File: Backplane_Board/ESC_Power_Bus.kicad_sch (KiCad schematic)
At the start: 18 parts, among them J21 Conn_01x02_Pin, SW2 SW_DPST_x2

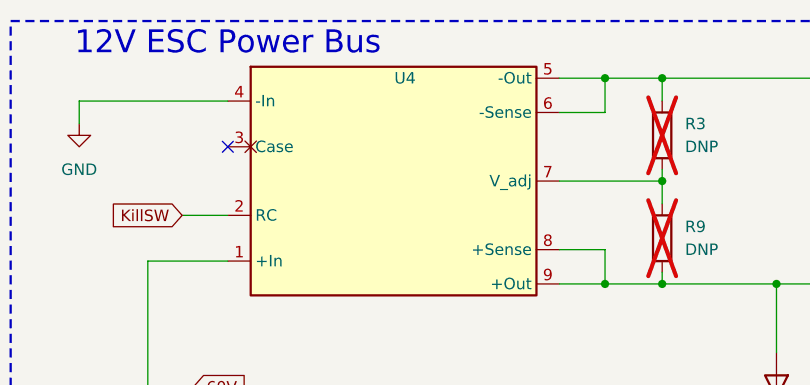
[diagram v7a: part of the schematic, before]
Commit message: updated i2c pullups to 3V3 logic, not isolator needed
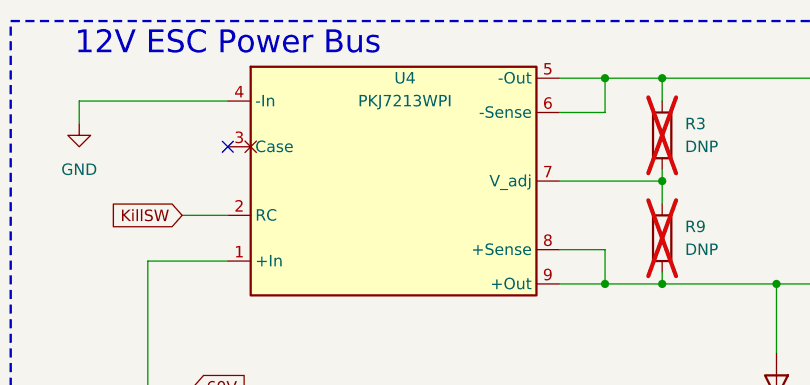
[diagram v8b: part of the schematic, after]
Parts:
- J21: footprint (none) -> Connector_PinHeader_2.54mm:PinHeader_1x02_P2.54mm_Vertical
- SW2: footprint (none) -> TerminalBlock:TerminalBlock_Xinya_XY308-2.54-2P_1x02_P2.54mm_Horizontal
- U4: value ~ -> PKJ7213WPI
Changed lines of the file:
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@@
 			)
 		)
-		(property "Footprint" ""
+		(property "Footprint" "TerminalBlock:TerminalBlock_Xinya_XY308-2.54-2P_1x02_P2.54mm_Horizontal"
 			(at 67.31 125.73 0)
 			(effects
@@
 			)
 		)
-		(property "Value" "~"
+		(property "Value" "PKJ7213WPI"
 			(at 60.325 27.94 0)
 			(effects
@@
 			)
 		)
-		(property "Datasheet" ""
+		(property "Datasheet" "https://flexpowermodules.com/resources/fpm-techspec-pkj7200w"
 			(at 59.69 36.83 0)
 			(effects
@@
 			)
 		)
-		(property "Description" ""
+		(property "Description" "PKJ 7200W series DC-DC Converters Input 14-160 V, Output up to 16.7 A / 200 W"
 			(at 59.69 36.83 0)
 			(effects
@@
 			)
 		)
-		(property "Footprint" ""
+		(property "Footprint" "Connector_PinHeader_2.54mm:PinHeader_1x02_P2.54mm_Vertical"
 			(at 55.88 175.26 0)
 			(effects
